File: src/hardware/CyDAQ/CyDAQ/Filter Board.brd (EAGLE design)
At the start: 160.9 x 110.9 mm, 214 parts, among them J1 DCJ0202, J10 Vout_HEADER, J11 5V0_SENSOR, J12 3V3_SENSOR, J13 1V8_SENSOR, J14 BRKOUT_JD, J15 BRKOUT_JC, J16 BRKOUT_JB, J17 BRKOUT_JF, J18 5V0_CONN, J19 3V3_CONN, J2 ZYBO_JF, J20 1V8_CONN, J21 BRKOUT_JD, J22 ZYBO_Power, J3 ZYBO_JE, J4 ZYBO_JD, J5 ZYBO_JC, J6 ZYBO_JB, J7 A_XADC, J8 SJ1-3523N, J9 Vin_HEADER, U1 TPS54531DDARDDA8_3P1X2P4-L, U10 CD74HCT4051, U11 CD74HCT4051, U12 OPA4197, U13 OPA4197, U14 OPA4197, U15 OPA4197, U16 OPA4197, U17 CD74HCT4053, U18 CD74HCT4051, U19 OPA2197, U3 TPS56339, U4 TPS56339, U5 LM43601PWPR, U6 X9258_A, U7 X925_B, U8 X9258_C, U9 X9258_D

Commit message: Adjusted notch filter values and uploaded BOM
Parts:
- C31: value 10uF -> 0.1uF
- C34, C35: value 5.6uF -> 0.1uF
- R39, R40: value 470 -> 39k
- R46: value 220 -> 9.1k
- R60, R65: value 50k -> 51k
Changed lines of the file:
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@@
 <drawing>
 <settings>
-<setting alwaysvectorfont="yes"/>
+<setting alwaysvectorfont="no"/>
 <setting verticaltext="up"/>
 </settings>
@@
 <attribute name="VALUE" x="74.8356" y="50.424" size="0.82" layer="27" font="vector" ratio="15" rot="R90" align="top-left"/>
 </element>
-<element name="R39" library="Resistors" library_urn="urn:adsk.eagle:library:4010572" package="0805" package3d_urn="urn:adsk.eagle:package:4010580/4" value="470" x="54.102" y="62.992" smashed="yes" rot="R270">
+<element name="R39" library="Resistors" library_urn="urn:adsk.eagle:library:4010572" package="0805" package3d_urn="urn:adsk.eagle:package:4010580/4" value="39k" x="54.102" y="62.992" smashed="yes" rot="R270">
 <attribute name="BOM" value="" x="104.648" y="127.254" size="1.778" layer="27" rot="R270" display="off"/>
 <attribute name="MPN" value="" x="104.648" y="127.254" size="1.778" layer="27" rot="R270" display="off"/>
@@
 <attribute name="VALUE" x="52.705" y="63.5" size="0.4064" layer="27" rot="R270"/>
 </element>
-<element name="R40" library="Resistors" library_urn="urn:adsk.eagle:library:4010572" package="0805" package3d_urn="urn:adsk.eagle:package:4010580/4" value="470" x="56.896" y="58.674" smashed="yes" rot="R270">
+<element name="R40" library="Resistors" library_urn="urn:adsk.eagle:library:4010572" package="0805" package3d_urn="urn:adsk.eagle:package:4010580/4" value="39k" x="56.896" y="58.674" smashed="yes" rot="R270">
 <attribute name="BOM" value="" x="107.442" y="129.54" size="1.778" layer="27" rot="R270" display="off"/>
 <attribute name="MPN" value="" x="107.442" y="129.54" size="1.778" layer="27" rot="R270" display="off"/>
@@
 <attribute name="VALUE" x="55.499" y="59.69" size="0.4064" layer="27" rot="R270"/>
 </element>
-<element name="R46" library="Resistors" library_urn="urn:adsk.eagle:library:4010572" package="0805" package3d_urn="urn:adsk.eagle:package:4010580/4" value="220" x="59.69" y="62.992" smashed="yes" rot="R270">
+<element name="R46" library="Resistors" library_urn="urn:adsk.eagle:library:4010572" package="0805" package3d_urn="urn:adsk.eagle:package:4010580/4" value="9.1k" x="59.69" y="62.992" smashed="yes" rot="R270">
 <attribute name="BOM" value="" x="110.236" y="156.972" size="1.778" layer="27" rot="R270" display="off"/>
 <attribute name="MPN" value="" x="110.236" y="156.972" size="1.778" layer="27" rot="R270" display="off"/>
@@
 <attribute name="VALUE" x="58.293" y="64.008" size="0.4064" layer="27" rot="R270"/>
 </element>
-<element name="C35" library="Capacitors" library_urn="urn:adsk.eagle:library:4010381" package="0805_H0.75" package3d_urn="urn:adsk.eagle:package:4010399/3" value="5.6uF" x="59.69" y="58.674" smashed="yes" rot="R270">
+<element name="C35" library="Capacitors" library_urn="urn:adsk.eagle:library:4010381" package="0805_H0.75" package3d_urn="urn:adsk.eagle:package:4010399/3" value="0.1uF" x="59.69" y="58.674" smashed="yes" rot="R270">
 <attribute name="BOM" value="" x="120.904" y="148.082" size="1.778" layer="27" rot="R270" display="off"/>
 <attribute name="MPN" value="" x="120.904" y="148.082" size="1.778" layer="27" rot="R270" display="off"/>
@@
 <attribute name="VALUE" x="58.293" y="59.69" size="0.4064" layer="27" rot="R270"/>
 </element>
-<element name="C34" library="Capacitors" library_urn="urn:adsk.eagle:library:4010381" package="0805_H0.75" package3d_urn="urn:adsk.eagle:package:4010399/3" value="5.6uF" x="56.896" y="62.992" smashed="yes" rot="R270">
+<element name="C34" library="Capacitors" library_urn="urn:adsk.eagle:library:4010381" package="0805_H0.75" package3d_urn="urn:adsk.eagle:package:4010399/3" value="0.1uF" x="56.896" y="62.992" smashed="yes" rot="R270">
 <attribute name="BOM" value="" x="118.11" y="152.4" size="1.778" layer="27" rot="R270" display="off"/>
 <attribute name="MPN" value="" x="118.11" y="152.4" size="1.778" layer="27" rot="R270" display="off"/>
@@
 <attribute name="VALUE" x="55.499" y="64.008" size="0.4064" layer="27" rot="R270"/>
 </element>
-<element name="C31" library="Capacitors" library_urn="urn:adsk.eagle:library:4010381" package="0805_H0.75" package3d_urn="urn:adsk.eagle:package:4010399/3" value="10uF" x="54.102" y="58.674" smashed="yes" rot="R90">
+<element name="C31" library="Capacitors" library_urn="urn:adsk.eagle:library:4010381" package="0805_H0.75" package3d_urn="urn:adsk.eagle:package:4010399/3" value="0.1uF" x="54.102" y="58.674" smashed="yes" rot="R90">
 <attribute name="BOM" value="" x="-7.112" y="-24.638" size="1.778" layer="27" rot="R90" display="off"/>
 <attribute name="MPN" value="" x="-7.112" y="-24.638" size="1.778" layer="27" rot="R90" display="off"/>
@@
 <attribute name="VALUE" x="130.429" y="55.372" size="0.4064" layer="27" rot="R270"/>
 </element>
-<element name="R60" library="Resistors" library_urn="urn:adsk.eagle:library:4010572" package="0805" package3d_urn="urn:adsk.eagle:package:4010580/4" value="50k" x="128.524" y="60.198" smashed="yes" rot="R180">
+<element name="R60" library="Resistors" library_urn="urn:adsk.eagle:library:4010572" package="0805" package3d_urn="urn:adsk.eagle:package:4010580/4" value="51k" x="128.524" y="60.198" smashed="yes" rot="R180">
 <attribute name="BOM" value="" x="271.78" y="6.096" size="1.778" layer="27" rot="R180" display="off"/>
 <attribute name="MPN" value="" x="271.78" y="6.096" size="1.778" layer="27" rot="R180" display="off"/>
@@
 <attribute name="VALUE" x="115.697" y="51.562" size="0.4064" layer="27" rot="R90"/>
 </element>
-<element name="R65" library="Resistors" library_urn="urn:adsk.eagle:library:4010572" package="0805" package3d_urn="urn:adsk.eagle:package:4010580/4" value="50k" x="111.506" y="59.944" smashed="yes" rot="R180">
+<element name="R65" library="Resistors" library_urn="urn:adsk.eagle:library:4010572" package="0805" package3d_urn="urn:adsk.eagle:package:4010580/4" value="51k" x="111.506" y="59.944" smashed="yes" rot="R180">
 <attribute name="BOM" value="" x="296.926" y="5.842" size="1.778" layer="27" rot="R180" display="off"/>
 <attribute name="MPN" value="" x="296.926" y="5.842" size="1.778" layer="27" rot="R180" display="off"/>

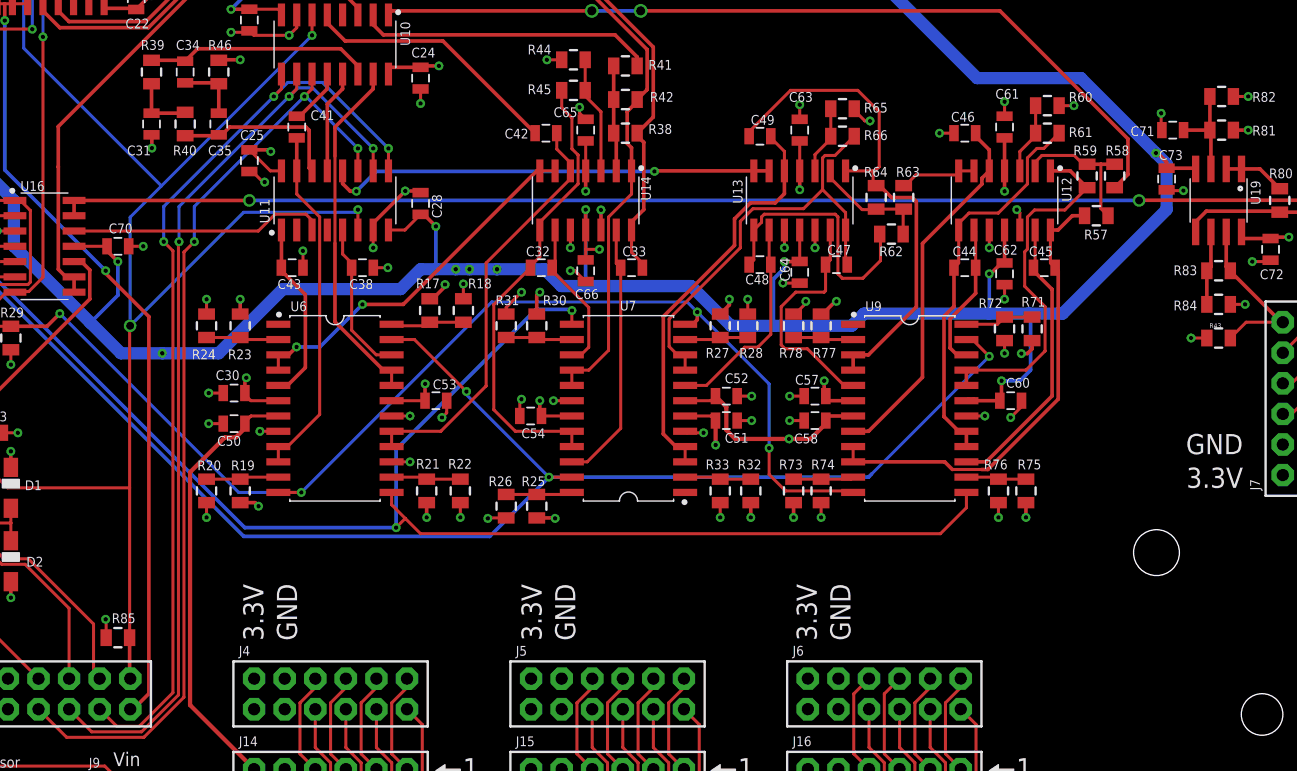
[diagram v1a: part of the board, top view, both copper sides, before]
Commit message: Fixed output MUX mapping
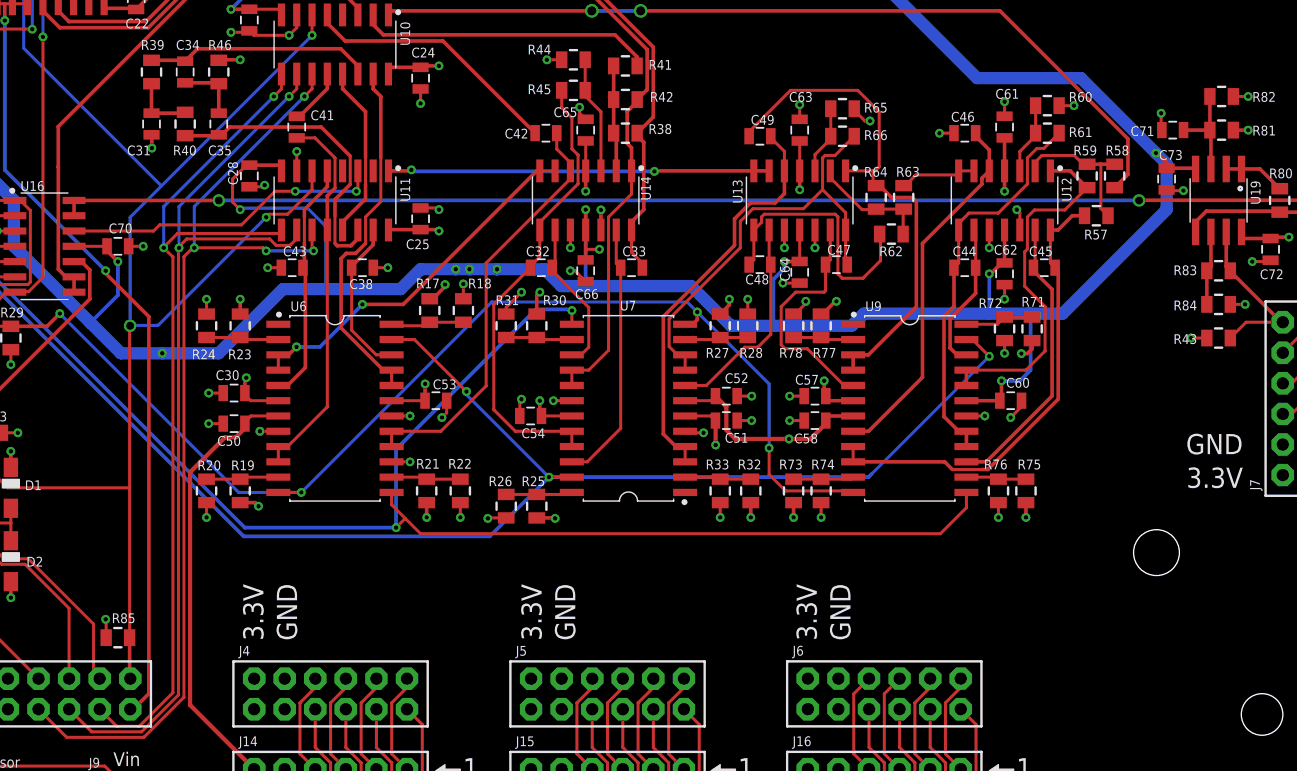
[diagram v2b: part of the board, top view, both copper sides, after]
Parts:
- moved C25 15.0 mm to (76.5, 50.8), turned to 90 degrees
- moved C28 14.4 mm to (62.2, 54.4), turned to 90 degrees
- turned C43 to 0 degrees
- turned U11 to 270 degrees
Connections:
- net BP2_OUT: now also U11.5; no longer U11.1
- net BP6_OUT: now also U11.1; no longer U11.12
- net HP1_OUT: now also U11.12; no longer U11.15
- net LP1_OUT: now also U11.15; no longer U11.5
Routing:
- net -5V0: track 395.5 -> 407.8 mm
- net NOTCH_OUT: track 14.2 -> 25.7 mm
- net PASSTHROUGH: track 8.57 -> 14.5 mm
- net BP6_OUT: track 37.5 -> 31.7 mm
- net N$43: track 21.4 -> 26.6 mm, vias 0 -> 2
- net BP2_OUT: track 15.2 -> 20.1 mm
- net GND: track 133.4 -> 128.9 mm
- net FILT_SELECT0: track 78.7 -> 82.5 mm, vias 3 -> 4
- net FILT_SELECT2: track 77.7 -> 74.2 mm, vias 3 -> 2
- net !SYSTEM_EN: track 137.0 -> 133.7 mm
- net HP1_OUT: track 29.6 -> 31.5 mm
- net +5V0: track 90.4 -> 89.4 mm
- net LP1_IN: track 29.5 -> 30.1 mm
- net FILT_SELECT1: track 78.0 -> 78.1 mm, vias 3 -> 2

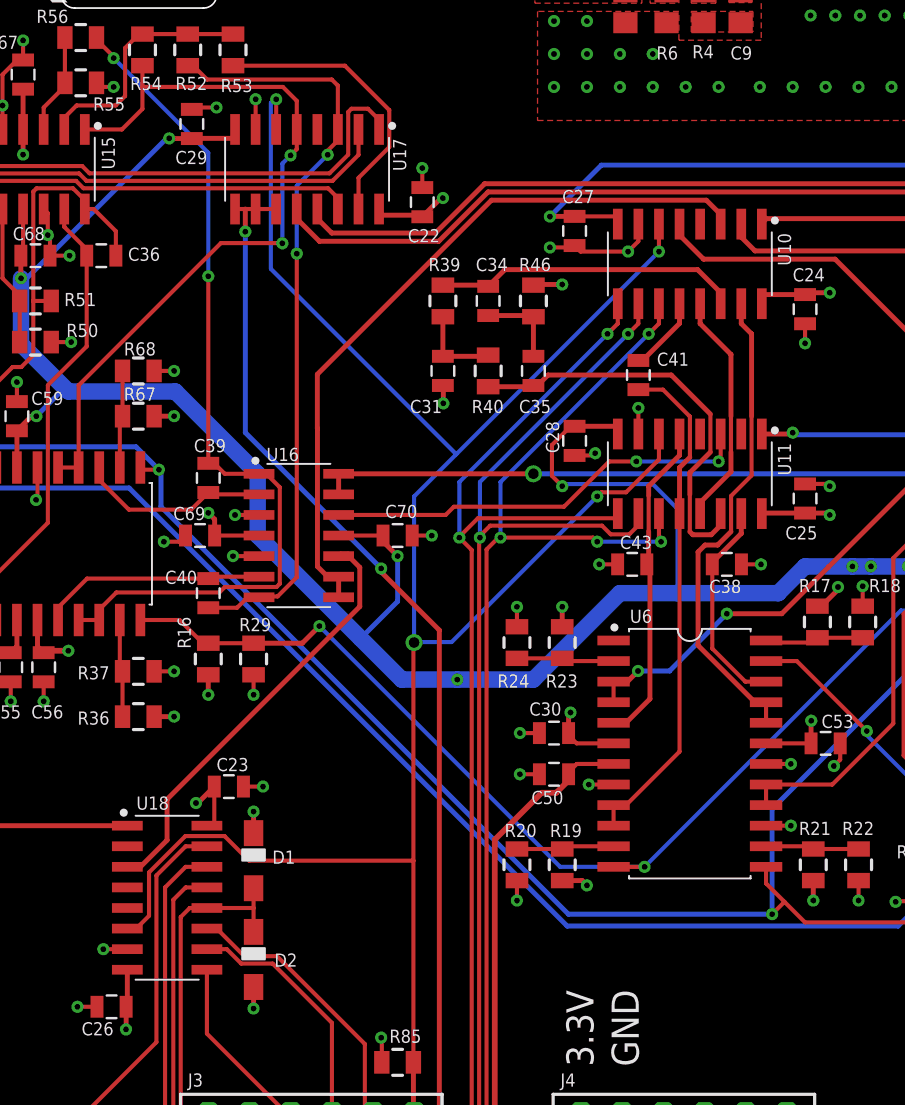
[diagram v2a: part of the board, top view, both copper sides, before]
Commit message: Started fixing pinout on MUXs
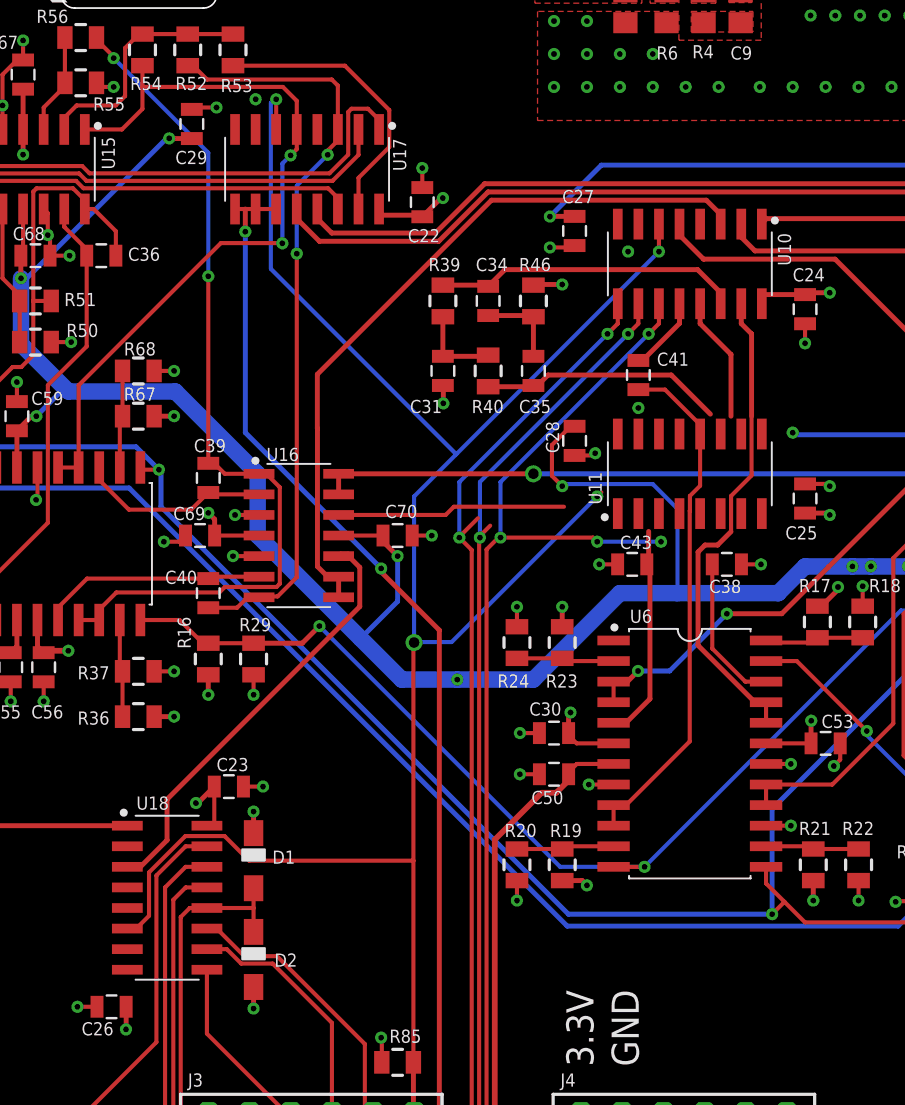
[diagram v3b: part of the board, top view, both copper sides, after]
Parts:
- turned U11 to 90 degrees
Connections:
- removed net HP/LP_OUT: U11.2
- net -5V0: now also U10.7, U11.7, U17.7, U18.7; no longer U10.8, U11.8, U17.8, U18.8
- net GND: now also U10.8, U11.8, U17.8, U18.8; no longer U10.7, U11.7, U17.7, U18.7
- net HP/LP6_OUT: now also U11.2
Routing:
- net N$43: track 26.6 -> 14.1 mm, vias 2 -> 0
- net -5V0: track 407.8 -> 396.3 mm
- net NOTCH_OUT: track 25.7 -> 15.0 mm
- net GND: track 128.9 -> 118.5 mm, vias 212 -> 211
- net FILT_SELECT1: track 78.1 -> 67.8 mm
- net FILT_SELECT2: track 74.2 -> 65.3 mm
- net PASSTHROUGH: track 14.5 -> 7.73 mm
- net BP2_OUT: track 20.1 -> 13.3 mm
- net !SYSTEM_EN: track 133.7 -> 127.8 mm
- net LP1_OUT: track 13.2 -> 9.48 mm
- net +5V0: track 89.4 -> 86.7 mm
- net BP6_OUT: track 31.7 -> 29.9 mm
- net FILT_SELECT0: track 82.5 -> 80.9 mm
- net HP1_OUT: track 31.5 -> 32.1 mm
